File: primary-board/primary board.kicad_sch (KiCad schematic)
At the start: 18 parts, among them J1 USB_C, J2 Sensor_Forward, J3 Sensor_Right, J4 Sensor_Left, J5 I2C Breakout, SW1 SW_SPST, SW2 SW_SPST, U1 ESP32-S3-1

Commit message: reorganized file tree swapped pushbuttons to smd
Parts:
- SW1, SW2: footprint Button_Switch_THT:SW_TH_Tactile_Omron_B3F-100x -> Button_Switch_SMD:SW_SPST_Omron_B3FS-101xP
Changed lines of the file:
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@@
 			)
 		)
-		(property "Footprint" "Button_Switch_THT:SW_TH_Tactile_Omron_B3F-100x"
+		(property "Footprint" "Button_Switch_SMD:SW_SPST_Omron_B3FS-101xP"
 			(at 121.92 55.88 0)
 			(effects
@@
 			)
 		)
-		(property "Footprint" "Button_Switch_THT:SW_TH_Tactile_Omron_B3F-100x"
+		(property "Footprint" "Button_Switch_SMD:SW_SPST_Omron_B3FS-101xP"
 			(at 121.92 76.2 0)
 			(effects
@@
 		)
 		(instances
-			(project "mcu board"
+			(project "primary board"
 				(path "/e926887c-cd26-4f47-be51-3352b14f6743"
 					(page "2")

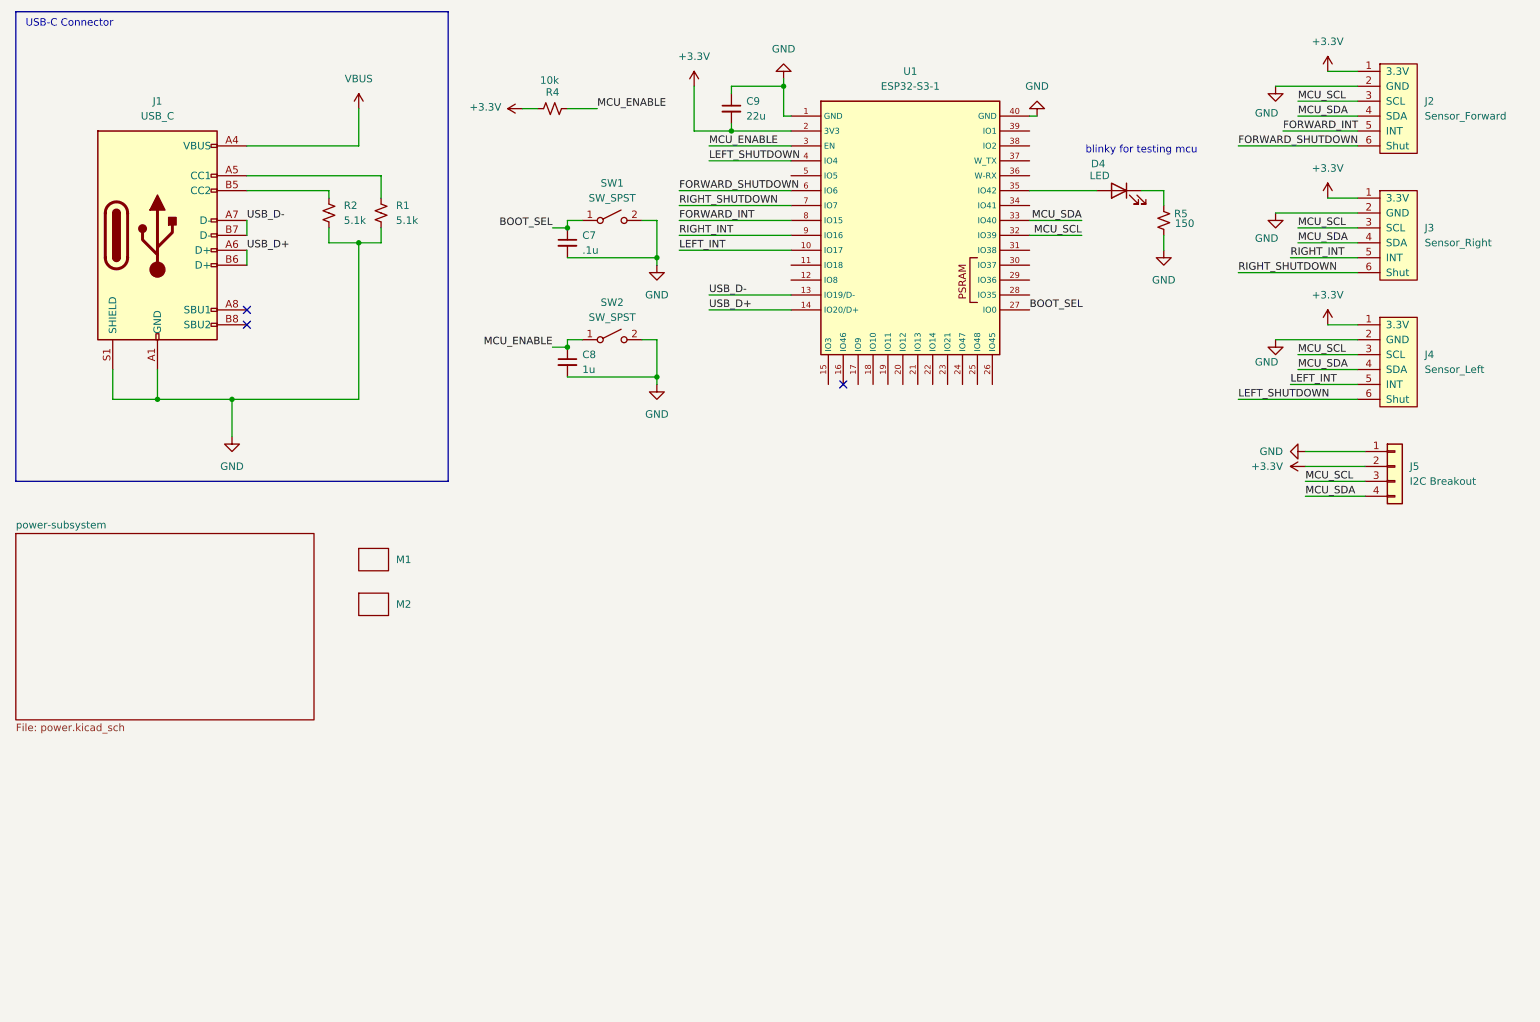
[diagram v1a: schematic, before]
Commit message: added motor connectors and h-bridge
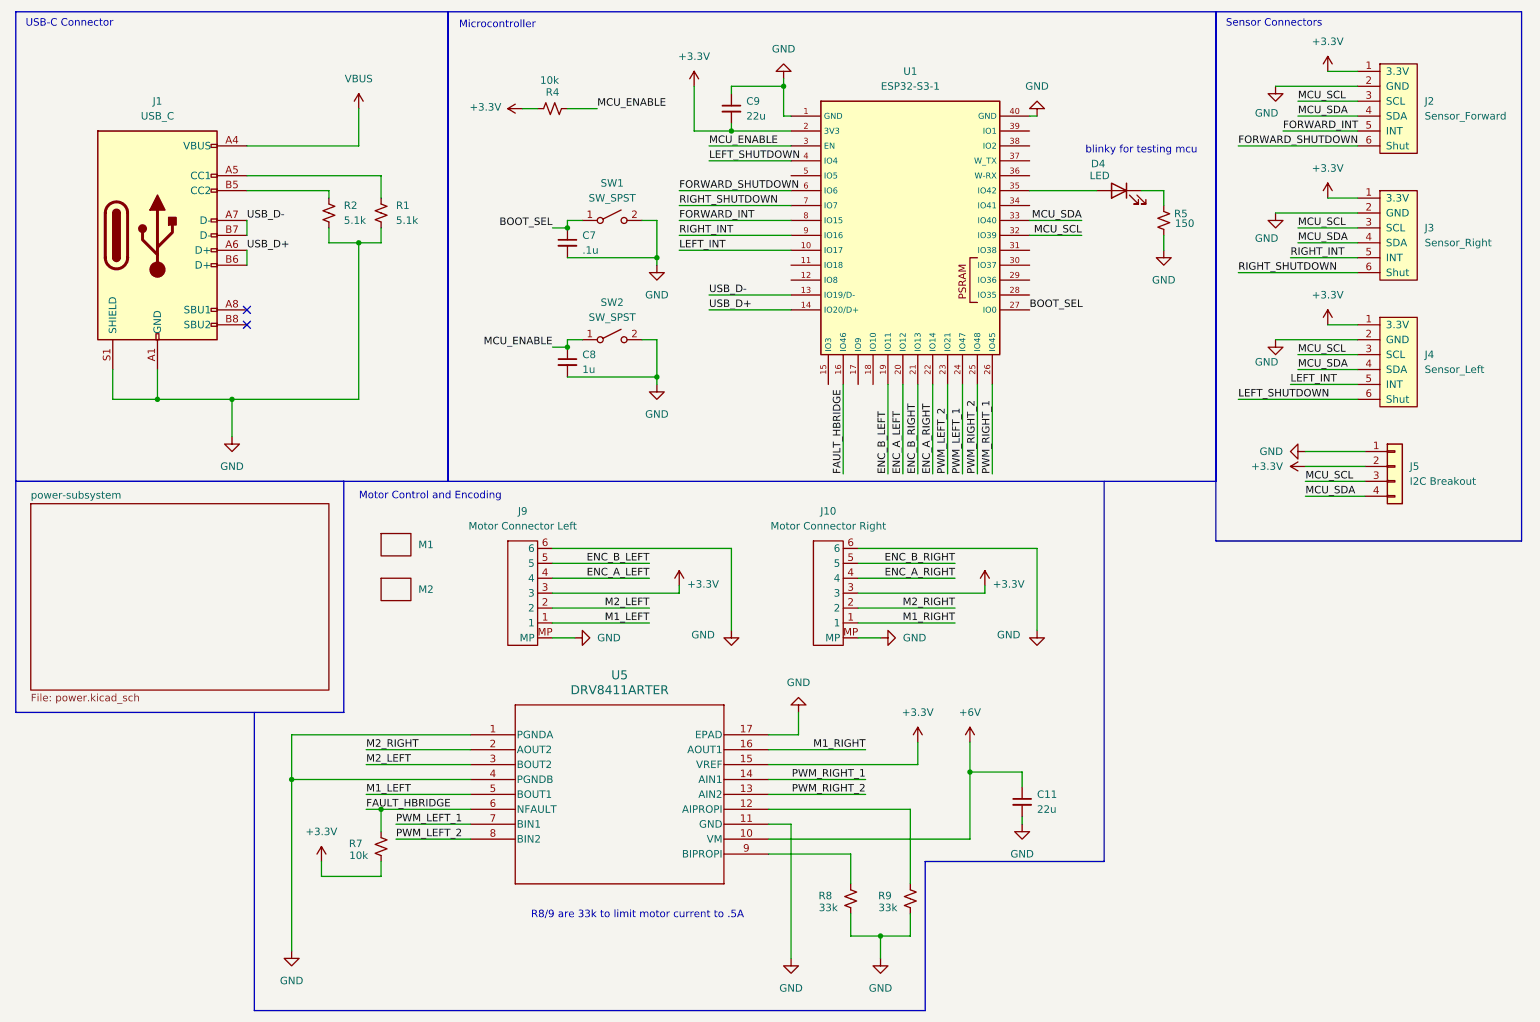
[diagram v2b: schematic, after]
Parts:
- added C11: 22u, Capacitor_SMD:C_0805_2012Metric, symbol Device:C_Small
- added J10: Motor Connector Right, mouseLib:JST_SH_6_V, symbol mouseLib:GeamMotorEnc_connector
- added J9: Motor Connector Left, mouseLib:JST_SH_6_V, symbol mouseLib:GeamMotorEnc_connector
- added R7: 10k, Resistor_SMD:R_0603_1608Metric, symbol Device:R_Small_US
- added R8, R9: 33k, Resistor_SMD:R_0603_1608Metric_Pad0.98x0.95mm_HandSolder, symbol Device:R_Small_US
- added U5: DRV8411ARTER, drv8411:WQFN16_RTE_TEX, symbol drv8411:DRV8411ARTER
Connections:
- net +3.3V: now also J10.3, J9.3, R7.2, U5.15 (VREF)
- net GND: now also C11.2, J10.6, J10.MP, J9.6, J9.MP, R8.2, R9.2, U5.1 (PGNDA), U5.11 (GND), U5.17 (EPAD), U5.4 (PGNDB)
- net FAULT_HBRIDGE: now reaches U1.16 (IO46)
- net FAULT_HBRIDGE: now also R7.1, U5.6 (NFAULT)
- net ENC_B_LEFT: now reaches U1.19 (IO11)
- net ENC_B_LEFT: now also J9.5
- net ENC_A_LEFT: now reaches U1.20 (IO12)
- net ENC_A_LEFT: now also J9.4
- net ENC_B_RIGHT: now reaches U1.21 (IO13)
- net ENC_B_RIGHT: now also J10.5
- net ENC_A_RIGHT: now reaches U1.22 (IO14)
- net ENC_A_RIGHT: now also J10.4
- net PWM_LEFT_2: now reaches U1.23 (IO21)
- net PWM_LEFT_2: now also U5.8 (BIN2)
- net PWM_LEFT_1: now reaches U1.24 (IO47)
- net PWM_LEFT_1: now also U5.7 (BIN1)
- net PWM_RIGHT_2: now reaches U1.25 (IO48)
- net PWM_RIGHT_2: now also U5.13 (AIN2)
- net PWM_RIGHT_1: now reaches U1.26 (IO45)
- net PWM_RIGHT_1: now also U5.14 (AIN1)
- new net: R9.1, U5.12 (AIPROPI)
- new net: R8.1, U5.9 (BIPROPI)
- new net +6V: C11.1, U5.10 (VM)
- new net M1_LEFT: J9.1, U5.5 (BOUT1)
- new net M1_RIGHT: J10.1, U5.16 (AOUT1)
- new net M2_LEFT: J9.2, U5.3 (BOUT2)
- new net M2_RIGHT: J10.2, U5.2 (AOUT2)
- no-connect marks 3 -> 2
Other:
- note added: "Microcontroller"
- note added: "Motor Control and Encoding"
- note added: "R8/9 are 33k to limit motor current to .5A"
- note added: "Sensor Connectors"
- moved on the sheet: M1, M2

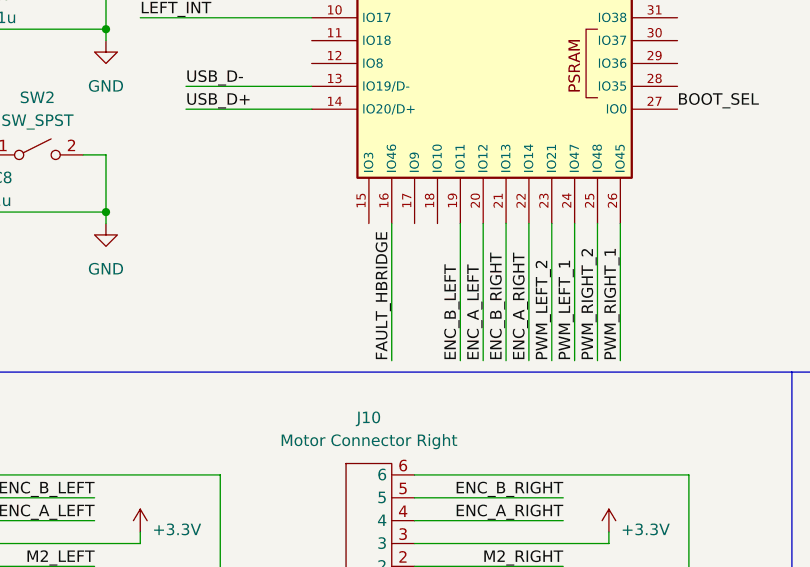
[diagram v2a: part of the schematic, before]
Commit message: complete board reroute. changed drv fault line into mcu. thickened all traces
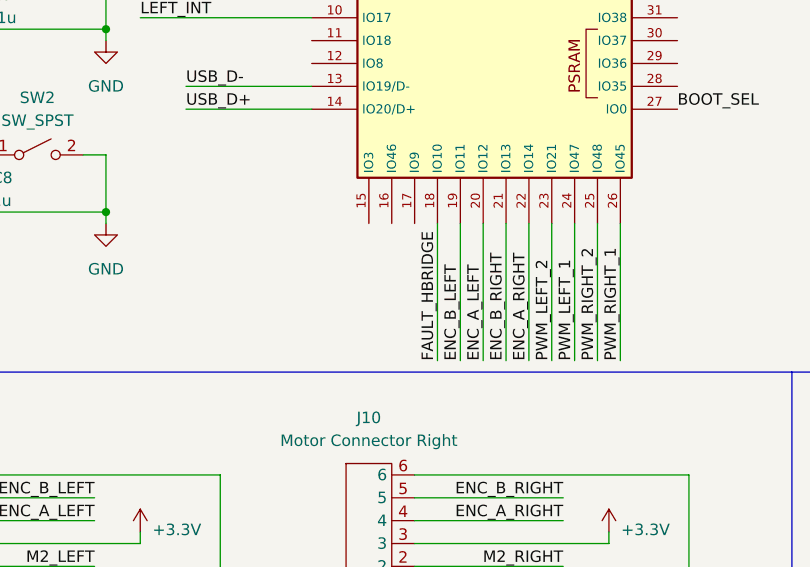
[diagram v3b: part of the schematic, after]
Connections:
- net FAULT_HBRIDGE: now also U1.18 (IO10); no longer U1.16 (IO46)
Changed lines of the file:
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@@
-	(wire
-		(pts
-			(xy 161.29 83.82) (xy 161.29 99.06)
-		)
-		(stroke
-			(width 0)
-			(type default)
-		)
-	)
 	(wire
 		(pts
@@
 		(pts
 			(xy 179.07 83.82) (xy 179.07 99.06)
+		)
+		(stroke
+			(width 0)
+			(type default)
+		)
+	)
+	(wire
+		(pts
+			(xy 166.37 83.82) (xy 166.37 99.06)
 		)
 		(stroke
@@
 	)
 	(label "FAULT_HBRIDGE"
-		(at 161.29 99.06 90)
-		(effects
-			(font
+		(at 166.37 99.06 90)
+		(effects
+			(font

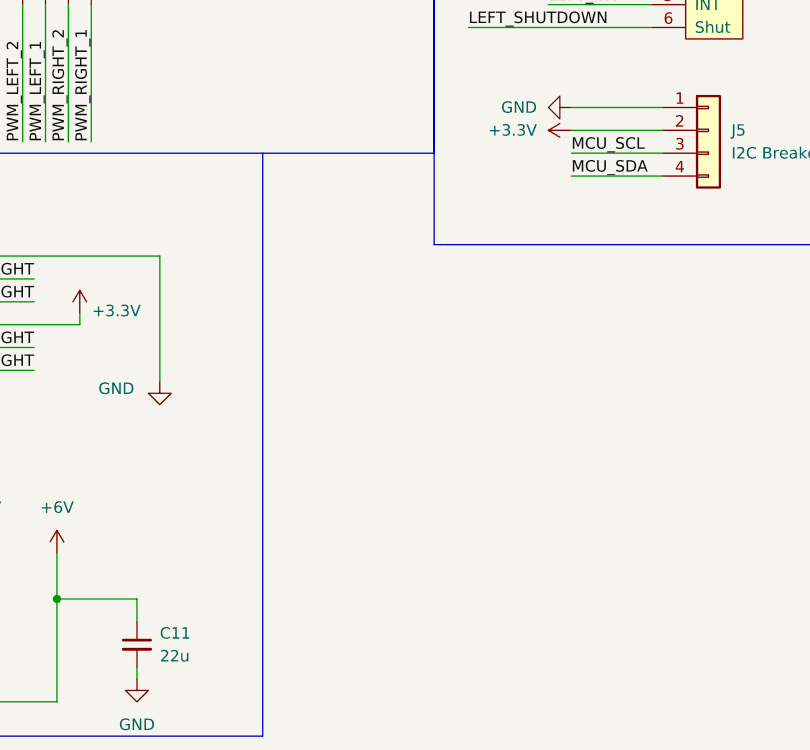
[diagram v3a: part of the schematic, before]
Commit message: added i2c pullups
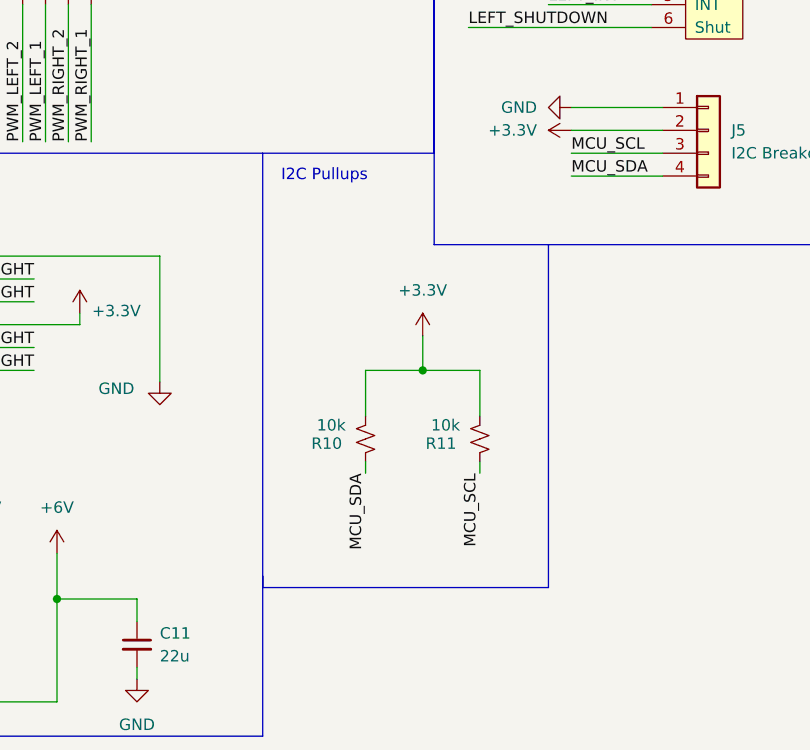
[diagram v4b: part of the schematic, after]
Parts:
- added R10, R11: 10k, Resistor_SMD:R_0603_1608Metric, symbol Device:R_Small_US
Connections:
- net +3.3V: now also R10.2, R11.2
- net MCU_SCL: now also R11.1
- net MCU_SDA: now also R10.1
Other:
- note added: "I2C Pullups"

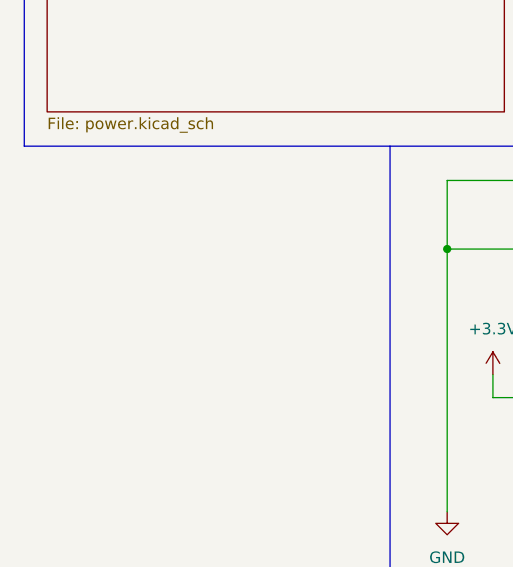
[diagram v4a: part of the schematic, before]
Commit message: adjusted drv8821 paste, added fiducials
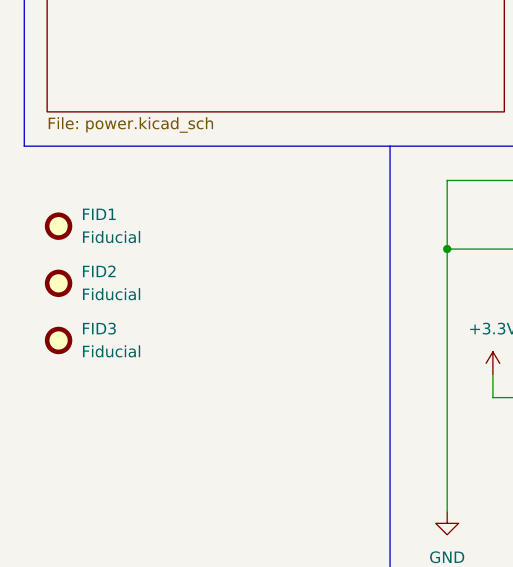
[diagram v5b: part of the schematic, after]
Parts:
- added FID1, FID2, FID3: Fiducial, Fiducial:Fiducial_0.5mm_Mask1mm, symbol Mechanical:Fiducial
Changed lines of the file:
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@@
+	)
+	(symbol
+		(lib_id "Mechanical:Fiducial")
+		(at 24.13 148.59 0)
+		(unit 1)
+		(exclude_from_sim no)
+		(in_bom no)
+		(on_board yes)
+		(dnp no)
+		(fields_autoplaced yes)
+		(property "Reference" "FID1"
+			(at 26.67 147.3199 0)
+			(effects
+				(font
+					(size 1.27 1.27)
+				)
+				(justify left)
+			)
+		)
+		(property "Value" "Fiducial"
+			(at 26.67 149.8599 0)
+			(effects
+				(font
+					(size 1.27 1.27)
+				)
+				(justify left)
+			)
+		)
+		(property "Footprint" "Fiducial:Fiducial_0.5mm_Mask1mm"
+			(at 24.13 148.59 0)
+			(effects
+				(font
+					(size 1.27 1.27)
+				)
+				(hide yes)
+			)
+		)
+		(property "Datasheet" "~"
+			(at 24.13 148.59 0)
+			(effects
+				(font
+					(size 1.27 1.27)
+				)
+				(hide yes)
+			)
+		)
+		(property "Description" "Fiducial Marker"
+			(at 24.13 148.59 0)
+			(effects
+				(font
+					(size 1.27 1.27)
+				)
+				(hide yes)
+			)
+		)
+		(instances
+			(project ""
+				(path "/e926887c-cd26-4f47-be51-3352b14f6743"
+					(reference "FID1")
+					(unit 1)
+				)
+			)
+		)
 	)
 	(symbol
@@
 	)
 	(symbol
+		(lib_id "Mechanical:Fiducial")
+		(at 24.13 154.94 0)
+		(unit 1)
+		(exclude_from_sim no)
+		(in_bom no)
+		(on_board yes)
+		(dnp no)
+		(fields_autoplaced yes)
+		(property "Reference" "FID2"
+			(at 26.67 153.6699 0)
+			(effects
+				(font
+					(size 1.27 1.27)
+				)
+				(justify left)
+			)
+		)
+		(property "Value" "Fiducial"
+			(at 26.67 156.2099 0)
+			(effects
+				(font
+					(size 1.27 1.27)
+				)
+				(justify left)
+			)
+		)
+		(property "Footprint" "Fiducial:Fiducial_0.5mm_Mask1mm"
+			(at 24.13 154.94 0)
+			(effects
+				(font
+					(size 1.27 1.27)
+				)
+				(hide yes)
+			)
+		)
+		(property "Datasheet" "~"
+			(at 24.13 154.94 0)
+			(effects
+				(font
+					(size 1.27 1.27)
+				)
+				(hide yes)
+			)
+		)
+		(property "Description" "Fiducial Marker"
+			(at 24.13 154.94 0)
+			(effects
+				(font
+					(size 1.27 1.27)
+				)
+				(hide yes)
+			)
+		)
+		(instances
+			(project "primary board"
+				(path "/e926887c-cd26-4f47-be51-3352b14f6743"
+					(reference "FID2")
+					(unit 1)
+				)
+			)
+		)
+	)
+	(symbol
 		(lib_id "power:GND")
 		(at 215.9 60.96 0)
@@
 					(unit 1)
 				)
+			)
+		)
+	)
+	(symbol
+		(lib_id "Mechanical:Fiducial")
+		(at 24.13 161.29 0)
+		(unit 1)
+		(exclude_from_sim no)
+		(in_bom no)
+		(on_board yes)
+		(dnp no)
+		(fields_autoplaced yes)
+		(property "Reference" "FID3"
+			(at 26.67 160.0199 0)
+			(effects
+				(font
+					(size 1.27 1.27)
+				)
+				(justify left)
+			)
+		)
+		(property "Value" "Fiducial"
+			(at 26.67 162.5599 0)
+			(effects
+				(font
+					(size 1.27 1.27)
+				)
+				(justify left)
+			)
+		)
+		(property "Footprint" "Fiducial:Fiducial_0.5mm_Mask1mm"
+			(at 24.13 161.29 0)
+			(effects
+				(font
+					(size 1.27 1.27)
+				)
+				(hide yes)
+			)
+		)
+		(property "Datasheet" "~"
+			(at 24.13 161.29 0)
+			(effects
+				(font
+					(size 1.27 1.27)
+				)
+				(hide yes)
+			)
+		)
+		(property "Description" "Fiducial Marker"
+			(at 24.13 161.29 0)
+			(effects
+				(font
+					(size 1.27 1.27)
+				)
+				(hide yes)
+			)
+		)
+		(instances
+			(project "primary board"
+				(path "/e926887c-cd26-4f47-be51-3352b14f6743"
+					(reference "FID3")
+					(unit 1)
+				)
